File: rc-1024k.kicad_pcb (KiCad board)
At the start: 2 copper layers, 99.1 x 49.9 mm, 14 parts, among them J1 RC2014, U1 SST39SF040, U2 AS6C4008, U3 74HCT138, U4 74HCT174, U5 74HCT32, U6 74HCT253

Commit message: Minor layout tweaks
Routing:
- net +5V: track 176.1 -> 195.7 mm
- net ~MREQ: track 67.8 -> 66.1 mm, vias 3 -> 2
- net ~ROM_CS: track 45.1 -> 46.0 mm
- net ~IOREQ: track 74.4 -> 73.7 mm

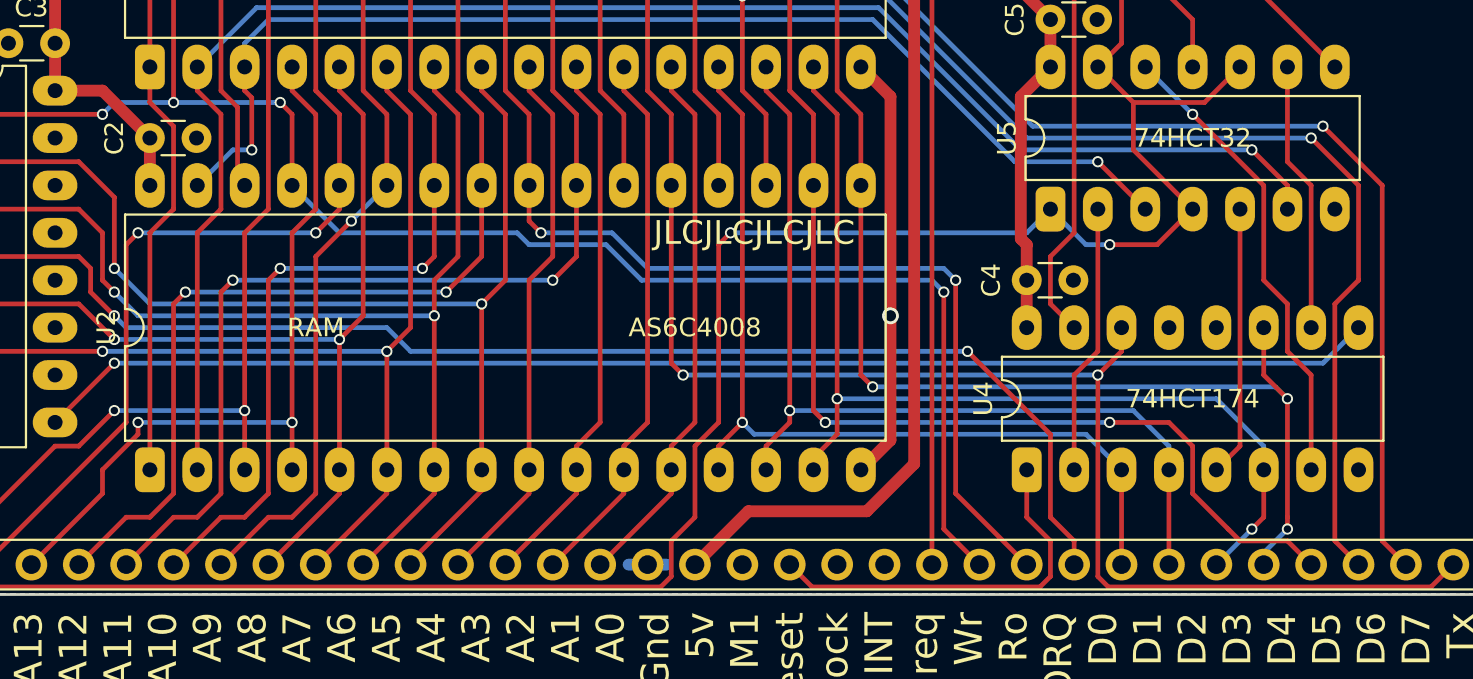
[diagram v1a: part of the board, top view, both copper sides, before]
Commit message: Rerouted datalines
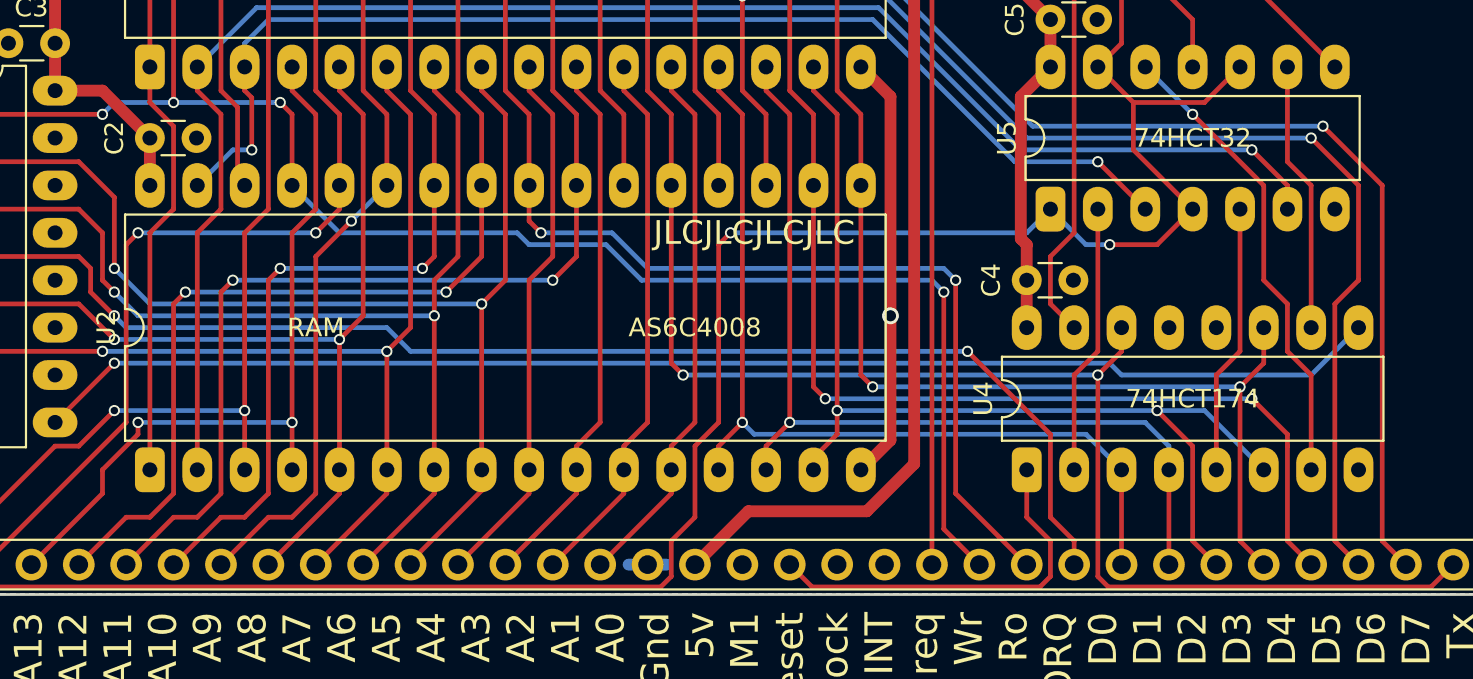
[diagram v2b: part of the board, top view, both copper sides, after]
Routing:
- net D3: track 69.9 -> 67.1 mm, vias 3 -> 2
- net D2: track 54.0 -> 56.4 mm
- net D4: track 66.3 -> 67.4 mm
- net /~CFG_CS: track 72.0 -> 72.5 mm

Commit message: Add icons
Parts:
- added Ref**: Val**, rc-1024k:Symbol-Dog-8mm, F.Cu at (242.6, 130.8)
- added Ref**: Val**, rc-1024k:Symbol-Dog-8mm, B.Cu at (242.6, 130.8)
- added Ref**: Val**, rc-1024k:Symbol-Pickle-8mm, F.Cu at (242.6, 123.2)
- added Ref**: Val**, rc-1024k:Symbol-Pickle-8mm, B.Cu at (242.6, 123.2)
